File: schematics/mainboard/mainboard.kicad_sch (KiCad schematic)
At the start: 38 parts, among them J1 ICSP, J2 USB_B_Micro, J3 DEALON DC-S050-200, J4 PWR_SELECT, J5 JOY1, J6 JOY2, J7 Conn_01x06_Pin, J8 DGAUGES, J9 LCD, U1 ATmega2560-16A, U2 FT232RL, U3 USBLC6-2P6, U4 AIP78M05, U5 L9110, Y1 16Mhz

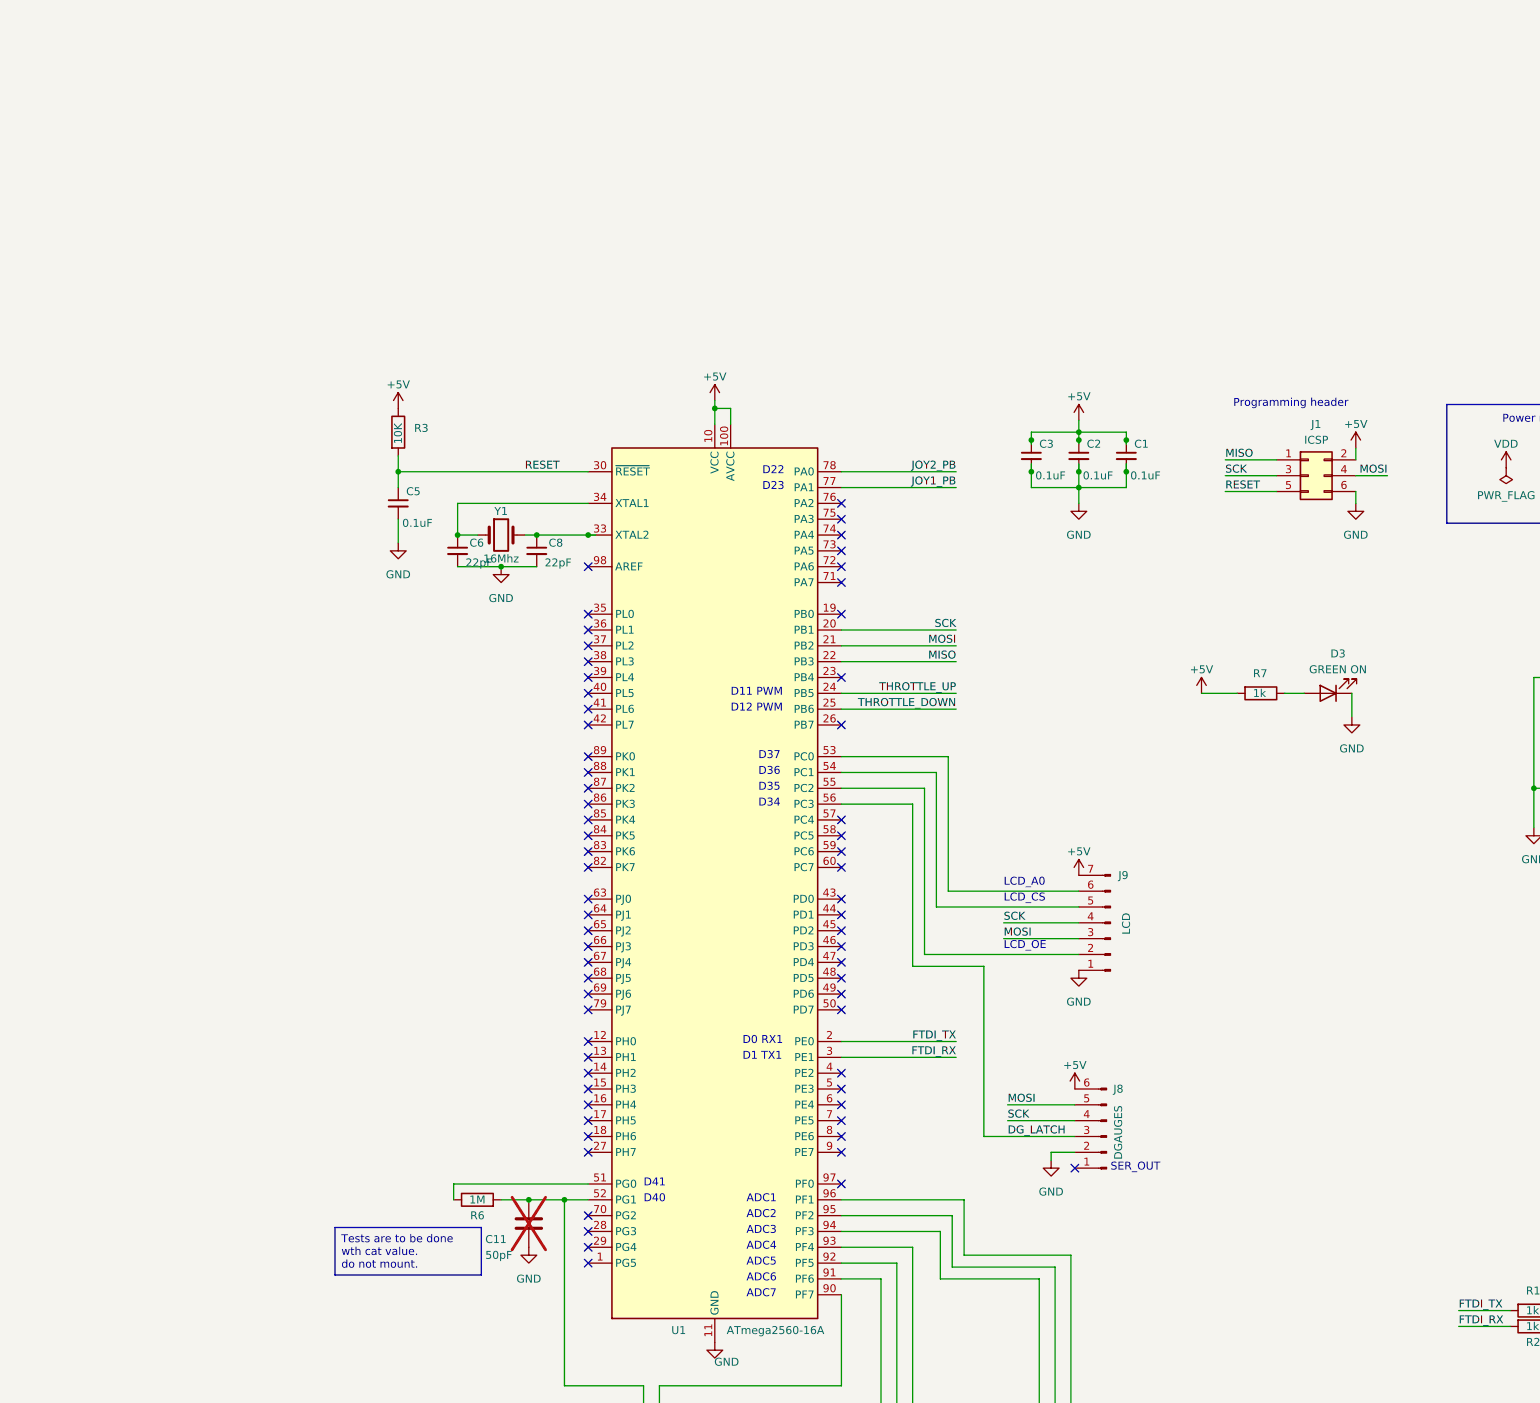
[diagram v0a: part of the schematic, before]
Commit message: SCH: Mainboard=> LED routing (1)
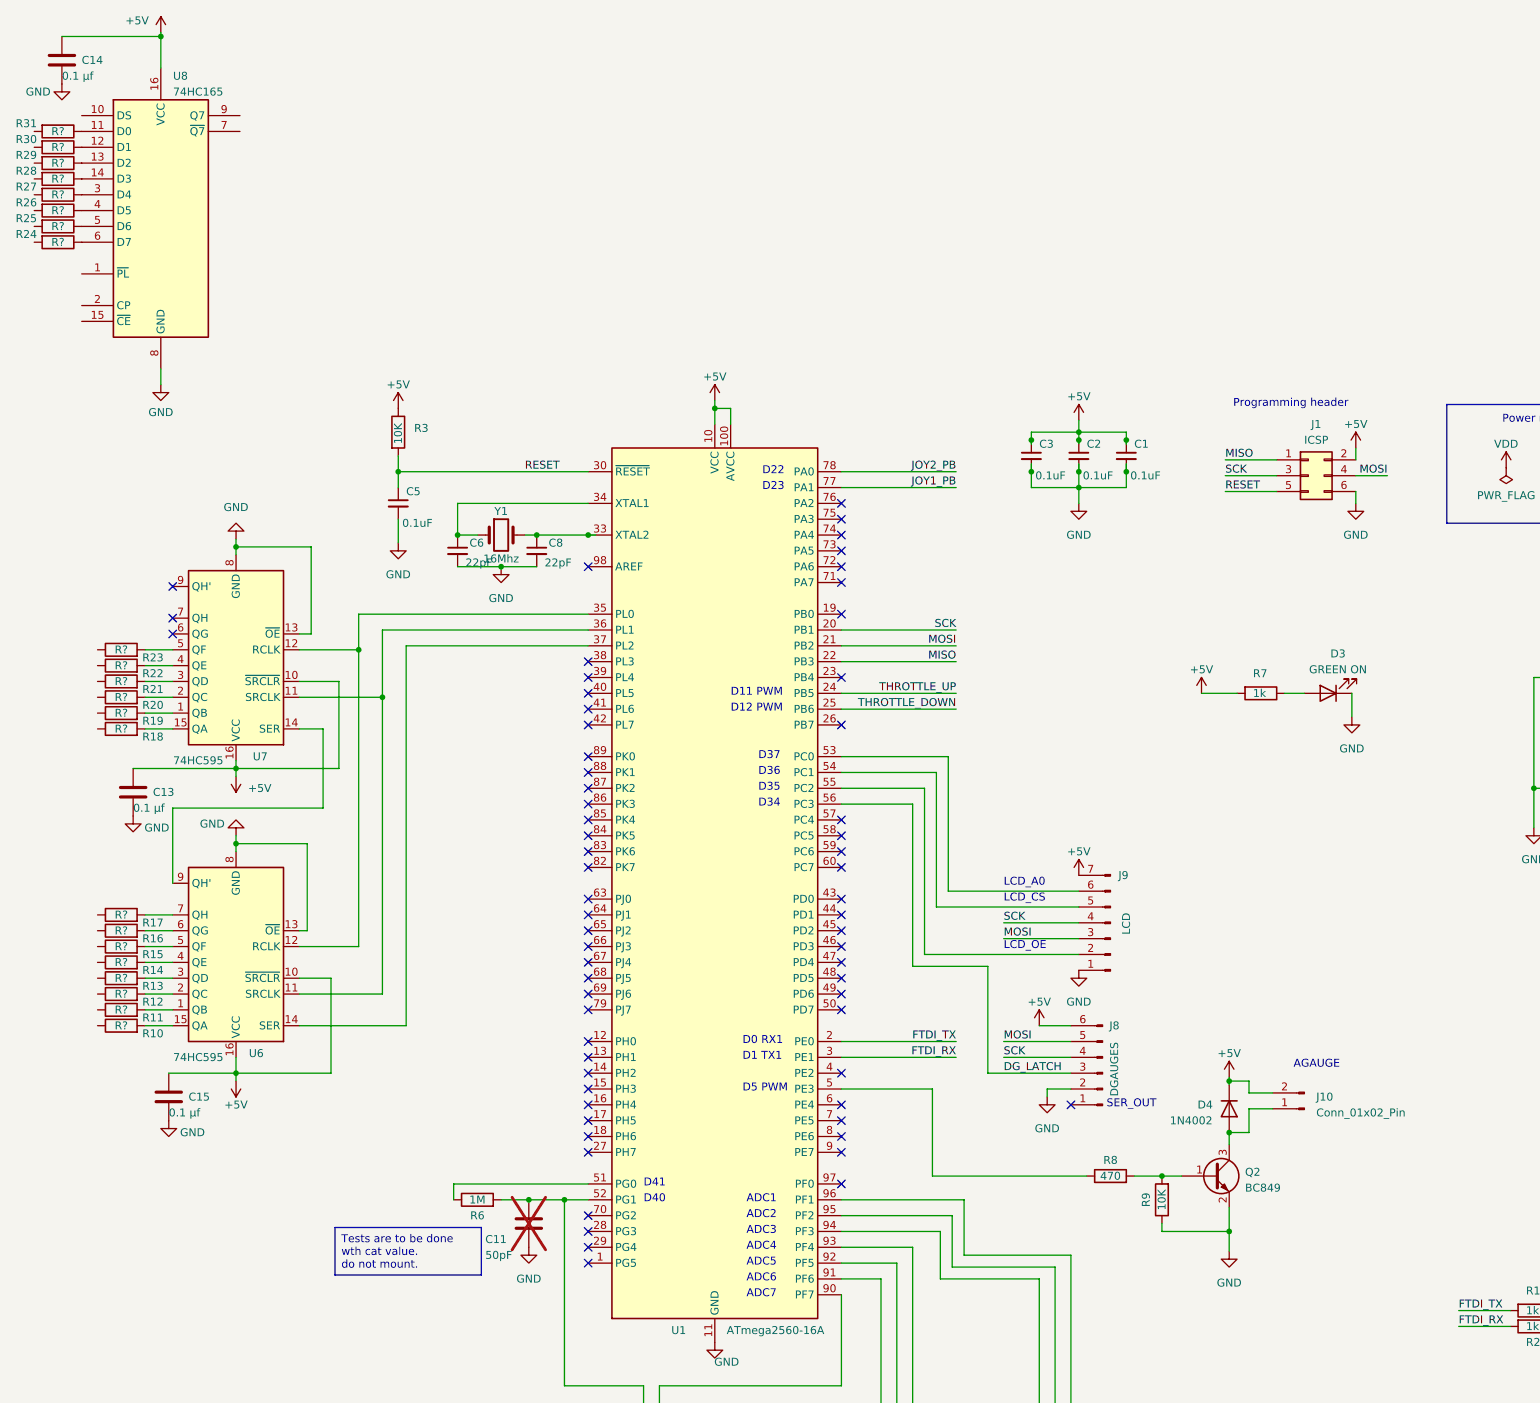
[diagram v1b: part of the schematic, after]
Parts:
- added C13, C14, C15: 0.1 µf, Capacitor_SMD:C_0603_1608Metric, symbol Device:C
- added D4: 1N4002, Diode_SMD:D_SOD-123F, symbol Diode:1N4002
- added J10: Conn_01x02_Pin, Connector_JST:JST_PH_B2B-PH-K_1x02_P2.00mm_Vertical, symbol Connector:Conn_01x02_Pin
- added Q2: BC849, Package_TO_SOT_SMD:SOT-23, symbol Transistor_BJT:BC849
- added R10, R11, R12, R13, R14, R15, R16, R17, R18, R19, R20, R21, R22, R23, R24, R25, R26, R27, R28, R29, R30, R31: R?, Resistor_SMD:R_0603_1608Metric, symbol Device:R
- added R8: 470, Resistor_SMD:R_0603_1608Metric, symbol Device:R
- added R9: 10K, Resistor_SMD:R_0603_1608Metric, symbol Device:R
- added U6, U7: 74HC595, Package_DIP:DIP-16_W7.62mm, symbol 74xx:74HC595
- added U8: 74HC165, Package_DIP:DIP-16_W7.62mm, symbol 74xx:74HC165
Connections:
- net +5V: now also C13.1, C14.1, C15.1, D4.1 (K), J10.2 (Pin_2), U6.10 (~{SRCLR}), U6.16 (VCC), U7.10 (~{SRCLR}), U7.16 (VCC), U8.16 (VCC)
- net GND: now also C13.2, C14.2, C15.2, Q2.2 (E), R9.1, U6.13 (~{OE}), U6.8 (GND), U7.13 (~{OE}), U7.8 (GND), U8.8 (GND)
- net at U1.35 (PL0): now also U6.12 (RCLK), U7.12 (RCLK)
- net at U1.36 (PL1): now also U6.11 (SRCLK), U7.11 (SRCLK)
- net at U1.37 (PL2): now also U6.14 (SER)
- net at U1.5 (PE3): now also R8.1
- new net: R21.2, U7.3 (QD)
- new net: R19.2, U7.1 (QB)
- new net: U6.9 (QH'), U7.14 (SER)
- new net: R18.2, U7.15 (QA)
- new net: R20.2, U7.2 (QC)
- new net: R22.2, U7.4 (QE)
- new net: R23.2, U7.5 (QF)
- new net: R25.1, U8.5 (D6)
- new net: R31.1, U8.11 (D0)
- new net: R28.1, U8.14 (D3)
- new net: R13.2, U6.3 (QD)
- new net: D4.2 (A), J10.1 (Pin_1), Q2.3 (C)
- new net: Q2.1 (B), R8.2, R9.2
- new net: R24.1, U8.6 (D7)
- new net: R11.2, U6.1 (QB)
- new net: R10.2, U6.15 (QA)
- new net: R12.2, U6.2 (QC)
- new net: R14.2, U6.4 (QE)
- new net: R15.2, U6.5 (QF)
- new net: R16.2, U6.6 (QG)
- new net: R17.2, U6.7 (QH)
- new net: R30.1, U8.12 (D1)
- new net: R29.1, U8.13 (D2)
- new net: R27.1, U8.3 (D4)
- new net: R26.1, U8.4 (D5)
- no-connect marks 78 -> 77
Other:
- note added: "AGAUGE"
- note added: "D5 PWM"
- moved on the sheet: J8

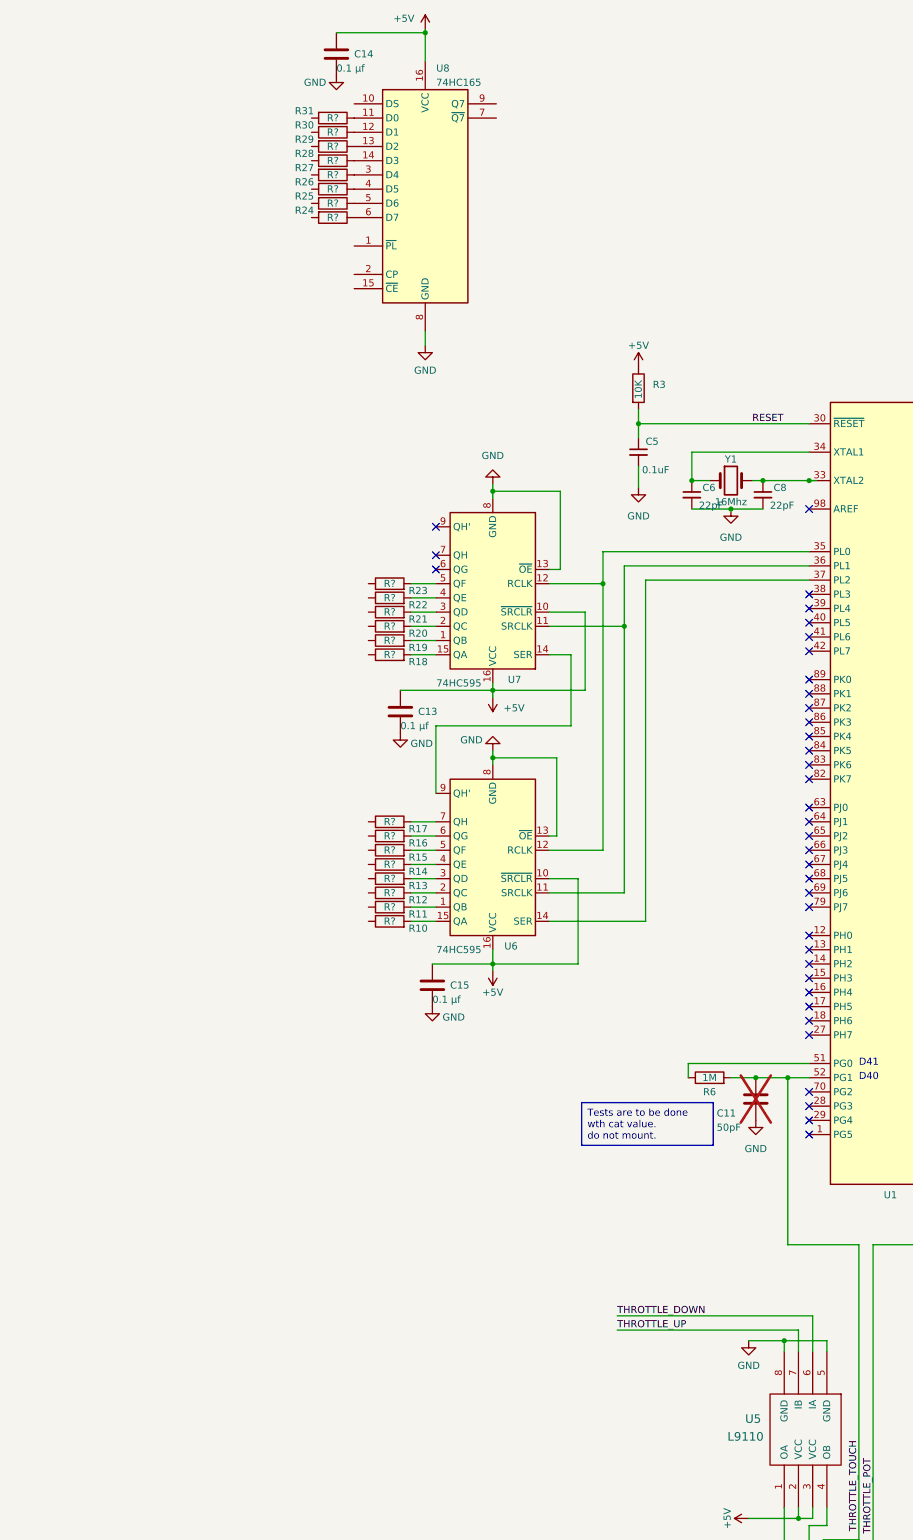
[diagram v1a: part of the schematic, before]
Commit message: SCH: Mainboard=> LED/Buttons routing(2)
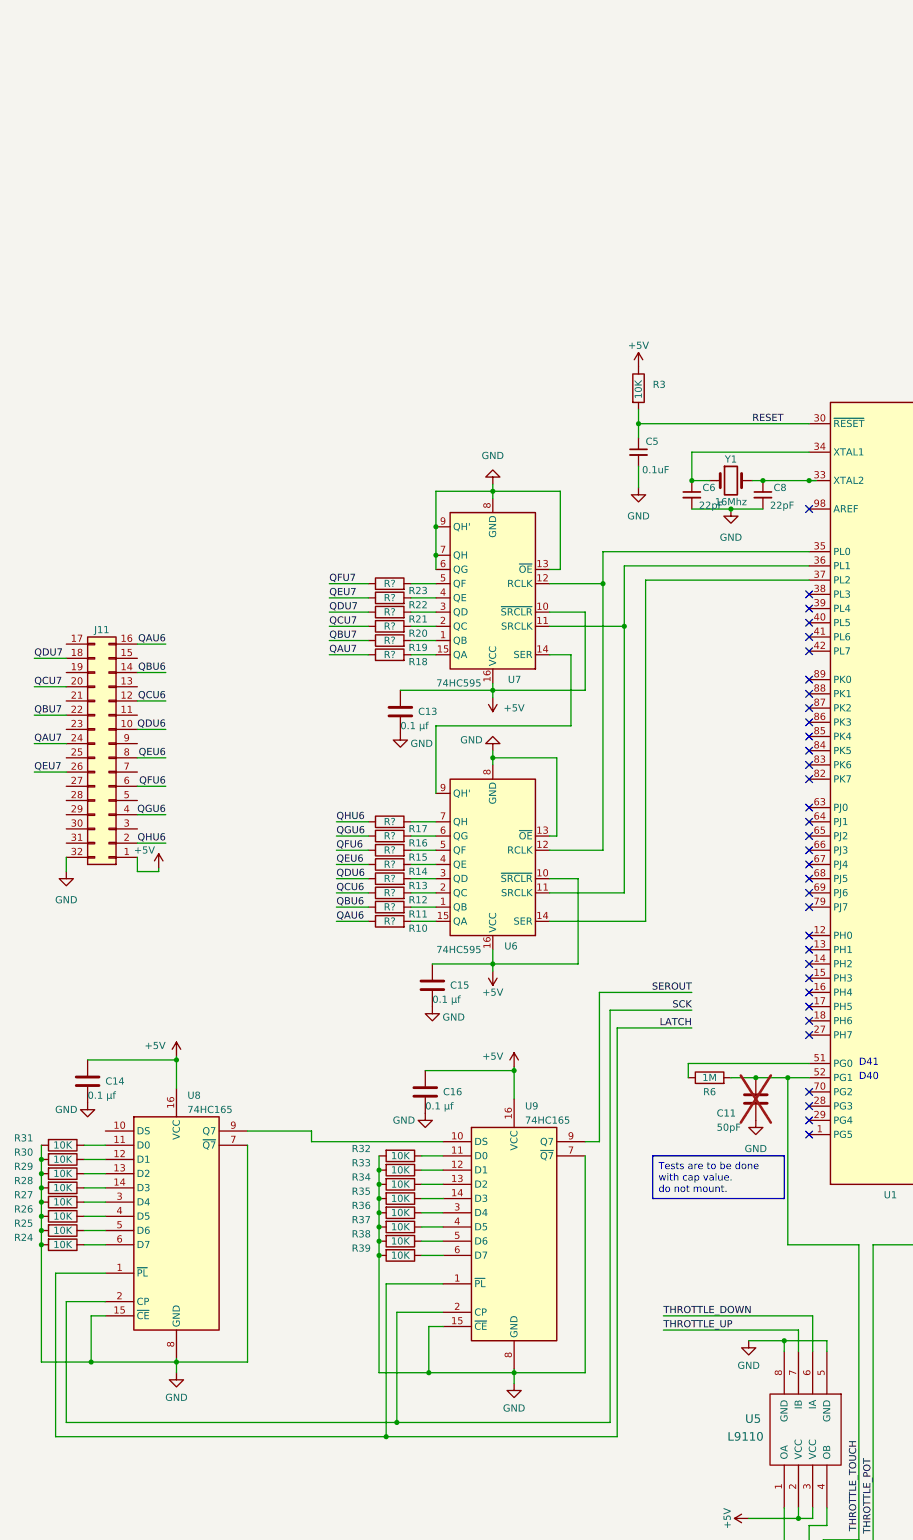
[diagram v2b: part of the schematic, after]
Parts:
- added C16: 0.1 µf, Capacitor_SMD:C_0603_1608Metric, symbol Device:C
- added J11: Conn_02x16_Counter_Clockwise, Connector_JST:JST_PHD_B32B-PHDSS_2x16_P2.00mm_Vertical, symbol Connector_Generic:Conn_02x16_Counter_Clockwise
- added R32, R33, R34, R35, R36, R37, R38, R39: 10K, Resistor_SMD:R_0603_1608Metric, symbol Device:R
- added U9: 74HC165, Package_DIP:DIP-16_W7.62mm, symbol 74xx:74HC165
- R24, R25, R26, R27, R28, R29, R30, R31: value R? -> 10K
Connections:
- net +5V: now also C16.1, J11.1 (Pin_1), U9.16 (VCC)
- net GND: now also R24.2, R25.2, R26.2, R27.2, R28.2, R29.2, R30.2, R31.2, U7.6 (QG), U7.7 (QH), U7.9 (QH'), U8.15 (~{CE}), U8.7 (~{Q7}), C16.2, J11.32 (Pin_32), R32.2, R33.2, R34.2, R35.2, R36.2, R37.2, R38.2, R39.2, U9.15 (~{CE}), U9.7 (~{Q7}), U9.8 (GND)
- net SCK: now also U8.2 (CP), U9.2 (CP)
- net QDU7: now reaches R21.1
- net QDU7: now also J11.18 (Pin_18)
- net QAU7: now reaches R18.1
- net QAU7: now also J11.24 (Pin_24)
- net QDU6: now reaches R13.1
- net QDU6: now also J11.10 (Pin_10)
- net LATCH: now reaches U8.1 (~{PL})
- net LATCH: now also U9.1 (~{PL})
- net at U8.9 (Q7): now also U9.10 (DS)
- net QGU6: now reaches R16.1
- net QGU6: now also J11.4 (Pin_4)
- net QEU7: now reaches R22.1
- net QEU7: now also J11.26 (Pin_26)
- net QBU7: now reaches R19.1
- net QBU7: now also J11.22 (Pin_22)
- net QAU6: now reaches R10.1
- net QAU6: now also J11.16 (Pin_16)
- net QBU6: now reaches R11.1
- net QBU6: now also J11.14 (Pin_14)
- net QCU6: now reaches R12.1
- net QCU6: now also J11.12 (Pin_12)
- net QHU6: now reaches R17.1
- net QHU6: now also J11.2 (Pin_2)
- net QCU7: now reaches R20.1
- net QCU7: now also J11.20 (Pin_20)
- net QFU6: now reaches R15.1
- net QFU6: now also J11.6 (Pin_6)
- net QEU6: now reaches R14.1
- net QEU6: now also J11.8 (Pin_8)
- net QFU7: now reaches R23.1
- new net: R38.1, U9.5 (D6)
- new net: R36.1, U9.3 (D4)
- new net: R33.1, U9.12 (D1)
- new net: R32.1, U9.11 (D0)
- new net: R37.1, U9.4 (D5)
- new net: R34.1, U9.13 (D2)
- new net: R35.1, U9.14 (D3)
- new net: R39.1, U9.6 (D7)
- new net SEROUT: U9.9 (Q7)
- no-connect marks 77 -> 74
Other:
- moved on the sheet: C14, R24, U8

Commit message: SCH: MAinboard=> Clean DRC issues
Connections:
- net LATCH is gone; now on net SAS_LATCH: U8.1 (~{PL}), U9.1 (~{PL})
- net QFU7 is gone; now on net U7Q5: R23.1
- net SEROUT is gone; now on net SAS_SEROUT: U9.9 (Q7)
- net GND: no longer U7.6 (QG), U7.7 (QH), U7.9 (QH'), U8.7 (~{Q7}), U9.7 (~{Q7})
- net SCK: no longer U8.2 (CP), U9.2 (CP)
- net U9D4: now reaches J11.11 (Pin_11)
- net U9D4: now also R36.1, U9.3 (D4)
- net U9D5: now reaches J11.13 (Pin_13)
- net U9D5: now also R37.1, U9.4 (D5)
- net U9D6: now reaches J11.15 (Pin_15)
- net U9D6: now also R38.1, U9.5 (D6)
- net U9D7: now reaches J11.17 (Pin_17)
- net U9D7: now also R39.1, U9.6 (D7)
- net U8D0: now reaches J11.19 (Pin_19)
- net U8D0: now also R24.1, U8.11 (D0)
- net U8D1: now reaches J11.21 (Pin_21)
- net U8D1: now also R25.1, U8.12 (D1)
- net U8D2: now reaches J11.23 (Pin_23)
- net U8D2: now also R26.1, U8.13 (D2)
- net U8D3: now reaches J11.25 (Pin_25)
- net U8D3: now also R27.1, U8.14 (D3)
- net U8D4: now reaches J11.27 (Pin_27)
- net U8D4: now also R28.1, U8.3 (D4)
- net U7Q5: now reaches J11.28 (Pin_28)
- net U8D5: now reaches J11.29 (Pin_29)
- net U8D5: now also R29.1, U8.4 (D5)
- net U9D0: now reaches J11.3 (Pin_3)
- net U9D0: now also R32.1, U9.11 (D0)
- net U8D6: now reaches J11.30 (Pin_30)
- net U8D6: now also R30.1, U8.5 (D6)
- net U8D7: now reaches J11.31 (Pin_31)
- net U8D7: now also R31.1, U8.6 (D7)
- net U9D1: now reaches J11.5 (Pin_5)
- net U9D1: now also R33.1, U9.12 (D1)
- net U9D2: now reaches J11.7 (Pin_7)
- net U9D2: now also R34.1, U9.13 (D2)
- net U9D3: now reaches J11.9 (Pin_9)
- net U9D3: now also R35.1, U9.14 (D3)
- net SAS_SEROUT: now reaches U1.38 (PL3)
- net SAS_SCK: now reaches U1.39 (PL4)
- net SAS_SCK: now also U8.2 (CP), U9.2 (CP)
- net SAS_LATCH: now reaches U1.40 (PL5)
- net QAU6 renamed U6Q0
- net QAU7 renamed U7Q0
- net QBU6 renamed U6Q1
- net QBU7 renamed U7Q1
- net QCU6 renamed U6Q2
- net QCU7 renamed U7Q2
- net QDU6 renamed U6Q3
- net QDU7 renamed U7Q3
- net QEU6 renamed U6Q4
- net QEU7 renamed U7Q4
- net QFU6 renamed U6Q5
- net QGU6 renamed U6Q6
- net QHU6 renamed U6Q7
- no-connect marks 74 -> 77
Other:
- note added: "SAS INPUTS"
- note added: "SAS LEDS"
- moved on the sheet: C1, C10, C11, C12, C13, C15, C16, C2, C3, C4, C5, C6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
